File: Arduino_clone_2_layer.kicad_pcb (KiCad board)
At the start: 2 copper layers, 42 x 29 mm, 17 parts, among them J1 Serial, J2 Digital pins, J3 I2C, J4 ICSP, U1 24LC1025, U2 24LC1025, U3 DS1337S+, U4 ATMEGA328P-AU, Y1 32 MHz, Y2 16 MHz

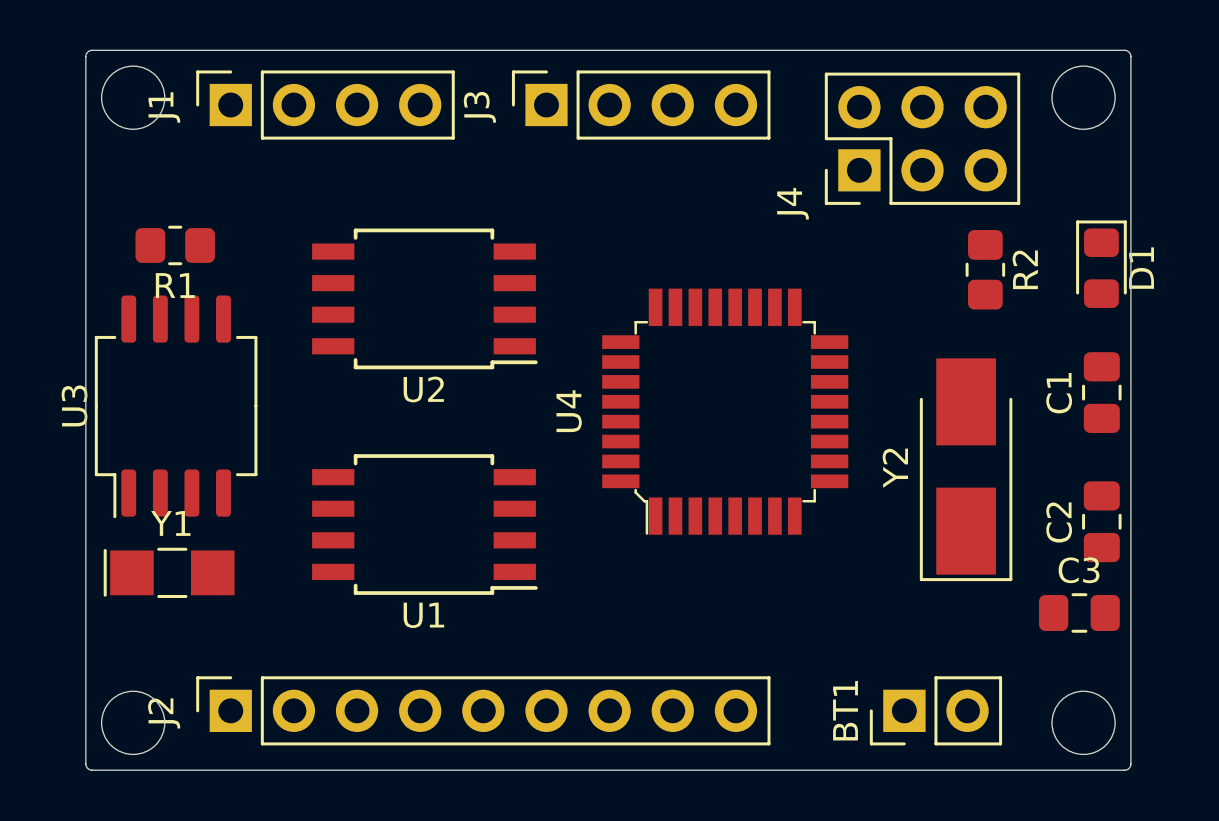
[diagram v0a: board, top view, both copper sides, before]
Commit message: 2-layer routing complete
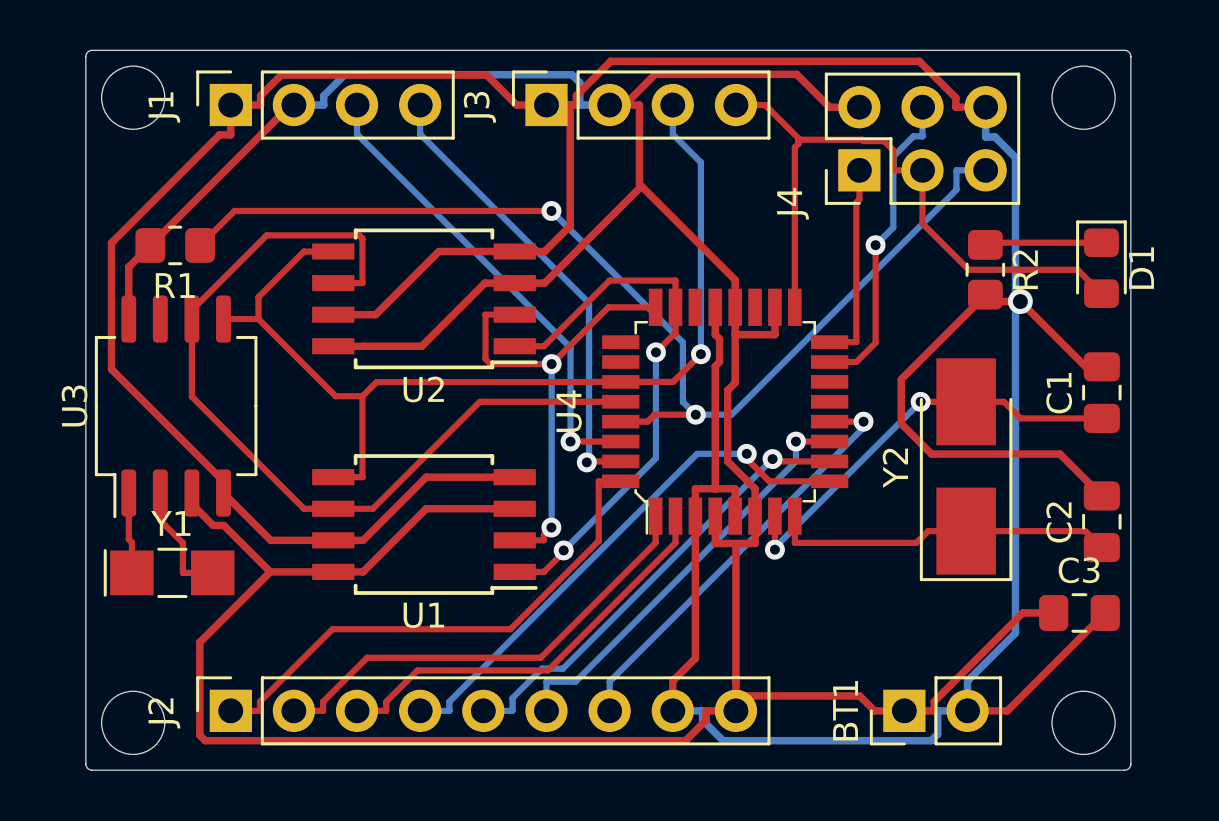
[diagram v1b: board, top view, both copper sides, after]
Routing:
- net GNDPWR: track 0.00 -> 170.7 mm, vias 0 -> 1
- net /Vcc: track 0.00 -> 145.2 mm
- net /RST: track 0.00 -> 44.6 mm, vias 0 -> 2
- net /SDA: track 0.00 -> 40.8 mm, vias 0 -> 1
- net /SCL: track 0.00 -> 35.5 mm
- net /SCK: track 0.00 -> 26.4 mm
- net /A0: track 0.00 -> 22.7 mm, vias 0 -> 2
- net /D5: track 0.00 -> 21.5 mm, vias 0 -> 1
- net /D2: track 0.00 -> 21.1 mm
- net /A1: track 0.00 -> 19.2 mm, vias 0 -> 2
- net /Rx: track 0.00 -> 19.1 mm, vias 0 -> 1
- net /D3: track 0.00 -> 18.6 mm
- net /Tx: track 0.00 -> 18.6 mm, vias 0 -> 1
- net /D6: track 0.00 -> 18.5 mm, vias 0 -> 1
- net Net-(C1-Pad1): track 0.00 -> 17.3 mm, vias 0 -> 2
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
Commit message: Added ground fill to 2-layer design
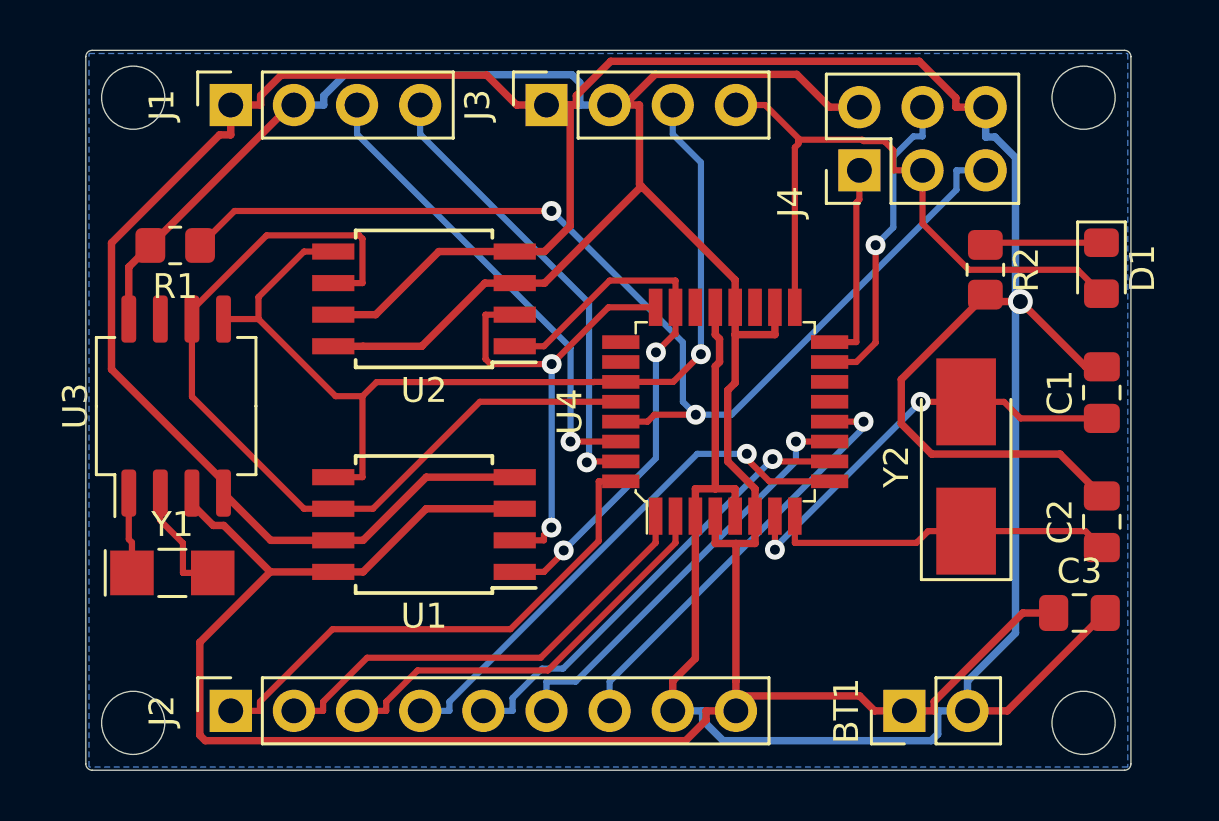
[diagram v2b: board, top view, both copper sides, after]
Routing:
- added copper zone on B.Cu, net GNDPWR
